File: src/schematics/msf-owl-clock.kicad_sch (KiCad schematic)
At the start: 55 parts, among them U001 BC805M, U002 TSOP75338TT

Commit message: Finalised various components and footprints.  Various tidy-ups.
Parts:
- added R017: 390Ω, restall-generic-resistors:nominal-0402-1005, symbol restall-generic-resistors:resistor
- CONN003: Manufacturer (none) -> Samtec; ManufacturerPartNumber (none) -> FTSH-105-01-L-DV-007-K
- CONN004: Manufacturer (none) -> Samtec; ManufacturerPartNumber (none) -> FTSH-110-01-F-DV-007-K
- LED001: footprint (none) -> restall-generic-leds:nominal-0603-1608; I_{F} ??mA_{typ} -> 20mA_{max}; Manufacturer (none) -> Harvatek; Manufacturer2 (none) -> Wurth Elektronik; Manufacturer2PartNumber (none) -> 150060RS75000; ManufacturerPartNumber (none) -> B1931USD-20D000814U1930; Package ??? -> 0603; V_{F} ?.?V_{typ} -> 2V_{typ}
- R004, R005, R007, R008, R009, R010, R011: value ??Ω -> 43Ω; Label ??Ω±1% 0.0625W -> 43Ω±1% 0.0625W
- R016: value 330Ω -> 390Ω; Label 330Ω±1% 0.0625W -> 390Ω±1% 0.0625W
- SPK001: value Speaker -> Header (Molex 502443-0270); footprint (none) -> restall-manufacturer-molex:502443-0270; Manufacturer (none) -> Molex; ManufacturerPartNumber (none) -> 502443-0270
- U001: footprint (none) -> restall-manufacturer-fanstel:BC805M
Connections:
- net 3-mcu-core/SDCARD_V_{DD}: now also R017.2
- net at LED001.2 (A), R016.1: now also R017.1
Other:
- note added: "R016-17"
- note added: "TODO: TFT CONNECTOR FOOTPRINTS..."
- note added: "The speaker should have a resonant frequency of less than 600Hz to cater for the lower-frequency bird sounds, such as the song of the tawny owl which has components around the 700Hz range. The speaker is connected to the PCB via a 2-pin header and pigtails. It is housed inside the clock's base / stand as that allows more freedom in the design of the cavity for better low-frequency response. This 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"
- note removed: "TODO: SELECT SPEAKER ! WILL PROBABLY NEED A SMALL ENCLOSURE OF SOME KIND (TO ABSORB THE OUT-OF-PHASE SOUND FROM BEHIND THE CONE AND ALLOW A DECENT LOW-FREQUENCY RESPONSE). MOUNTING ALSO NEEDS TO BE CONSIDERED - PREFERABLY ON THE BACK BUT WITH DIRECTION TO THE SIDE OR FRONT FOR BETTER AUDIO PROJECTION. PROBABLY A PART TO BUY AND/OR ASSEMBLE SEPARATELY RATHER THEN SEND FOR PCBA, SINCE NOT MANY SPEA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"
- moved on the sheet: LED001, SPK001

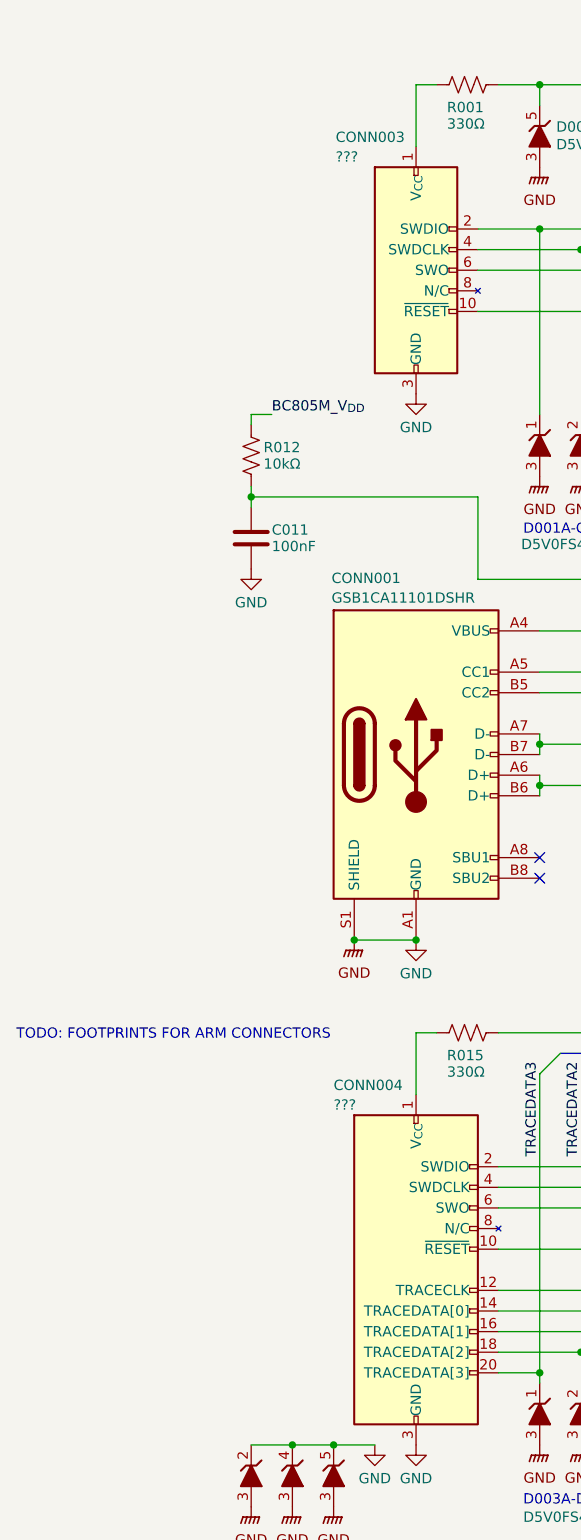
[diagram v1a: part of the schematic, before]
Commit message: Added footprints for the ARM debug connectors.  Added a datasheet for the speaker connector (Molex 502443-0270).
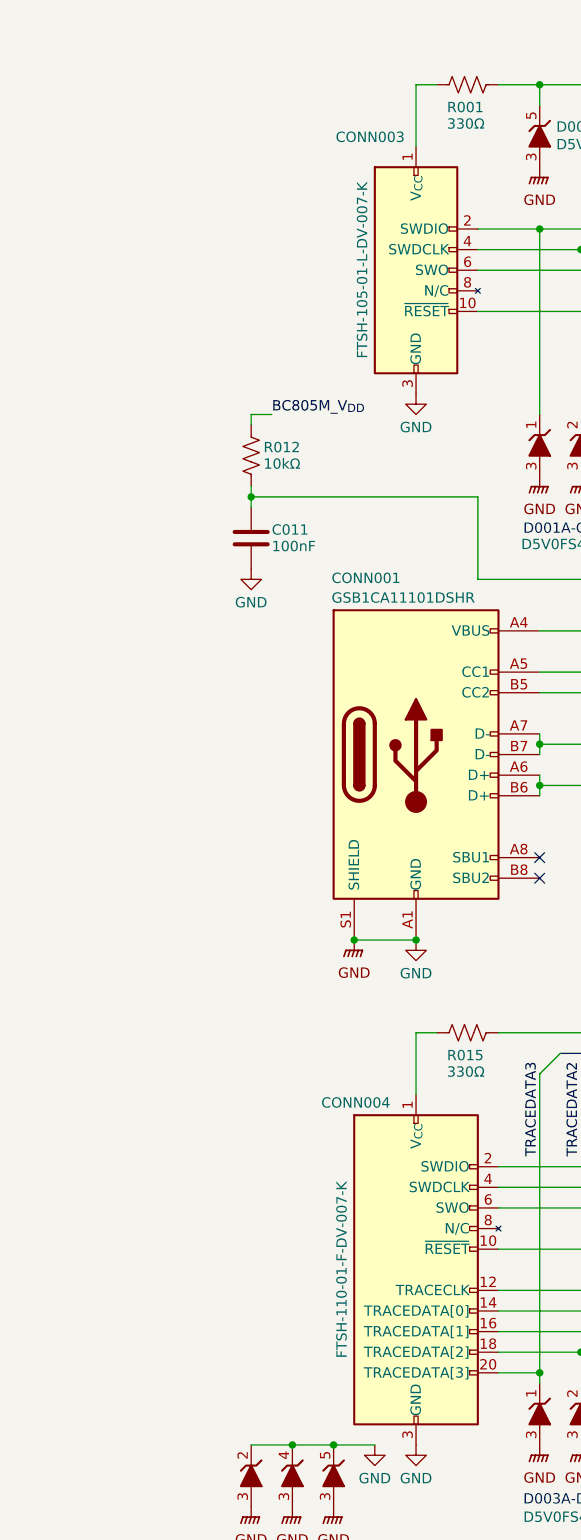
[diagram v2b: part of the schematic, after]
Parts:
- CONN003: footprint (none) -> restall-manufacturer-samtec:FTSH-105-?-?-DV-007-?-?; Package ??? -> FTSH-105-01-L-DV-007-K
- CONN004: footprint (none) -> restall-manufacturer-samtec:FTSH-110-01-?-DV-007-?-?; Package ??? -> FTSH-110-01-F-DV-007-K
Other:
- note removed: "TODO: FOOTPRINTS FOR ARM CONNECTORS"
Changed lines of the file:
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@@
     (effects (font (size 1.27 1.27)) (justify left bottom))
   )
-  (text "TODO: FOOTPRINTS FOR ARM CONNECTORS" (at -11.176 133.096 0)
-    (effects (font (size 1.27 1.27)) (justify left bottom))
-  )
   (text "TODO: DOUBLE-CHECK THESE PIN NUMBERS - THEY LOOK CORRECT BUT TRY AN ACTUAL CONNECTION (1 -> 12, 24 -> 13"
     (at 327.406 36.322 0)
@@
       (effects (font (size 1.27 1.27)) (justify left) hide)
     )
-    (property "Footprint" "" (at 38.1 34.29 0)
+    (property "Footprint" "restall-manufacturer-samtec:FTSH-105-?-?-DV-007-?-?" (at 38.1 34.29 0)
       (effects (font (size 1.27 1.27)) (justify left) hide)
     )
@@
       (effects (font (size 1.27 1.27)) (justify left) hide)
     )
-    (property "Package" "???" (at 28.194 24.13 0)
-      (effects (font (size 1.27 1.27)) (justify left))
+    (property "Package" "FTSH-105-01-L-DV-007-K" (at 31.496 38.1 90)
+      (effects (font (size 1.27 1.27)))
     )
     (property "Manufacturer" "Samtec" (at 38.1 33.02 0)
@@
   (symbol (lib_id "restall-manufacturer-arm:arm-cortex-m-debug-etm-header-2x10") (at 38.1 161.29 0) (unit 1)
     (in_bom yes) (on_board yes) (dnp no)
-    (property "Reference" "CONN004" (at 27.94 138.5458 0)
+    (property "Reference" "CONN004" (at 26.416 140.716 0)
       (effects (font (size 1.27 1.27)) (justify left))
     )
@@
       (effects (font (size 1.27 1.27)) (justify left) hide)
     )
-    (property "Footprint" "" (at 38.1 157.48 0)
+    (property "Footprint" "restall-manufacturer-samtec:FTSH-110-01-?-DV-007-?-?" (at 38.1 157.48 0)
       (effects (font (size 1.27 1.27)) (justify left) hide)
     )
@@
       (effects (font (size 1.27 1.27)) (justify left) hide)
     )
-    (property "Package" "???" (at 27.94 140.97 0)
-      (effects (font (size 1.27 1.27)) (justify left))
+    (property "Package" "FTSH-110-01-F-DV-007-K" (at 28.956 161.29 90)
+      (effects (font (size 1.27 1.27)))
     )
     (property "Manufacturer" "Samtec" (at 38.1 156.21 0)

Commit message: Added the USB connector footprint.
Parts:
- CONN001: footprint (none) -> restall-manufacturer-amphenol:GSB1CA11101DSHR
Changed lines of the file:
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@@
       (effects (font (size 1.27 1.27)) (justify left) hide)
     )
-    (property "Footprint" "" (at 44.45 116.84 0)
+    (property "Footprint" "restall-manufacturer-amphenol:GSB1CA11101DSHR" (at 44.45 116.84 0)
       (effects (font (size 1.27 1.27)) (justify left) hide)
     )

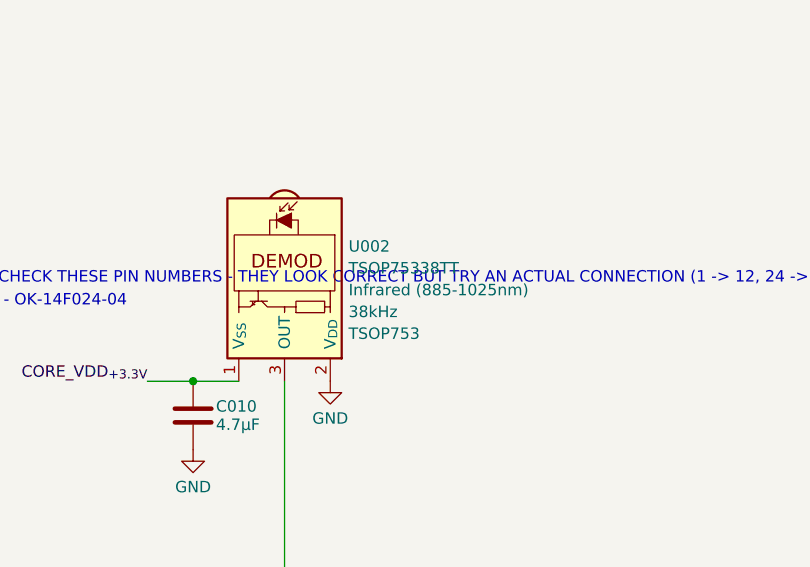
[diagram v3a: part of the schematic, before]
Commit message: Fixed the orientation of the TSOP75338TT.
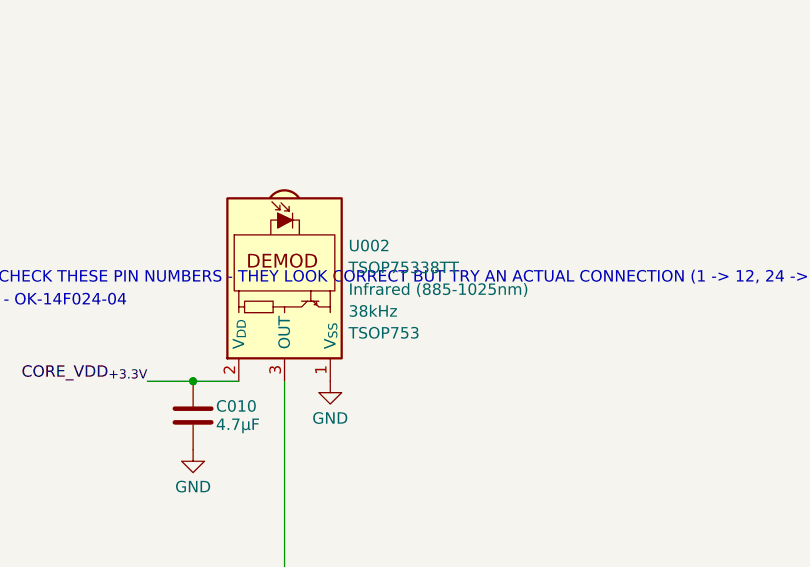
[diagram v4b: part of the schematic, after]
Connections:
- net CORE_VDD_{+3.3V}: now also U002.2 (V_{DD}); no longer U002.1 (V_{SS}), U002.4 (V_{SS})
- net GND: now also U002.1 (V_{SS}), U002.4 (V_{SS}); no longer U002.2 (V_{DD})
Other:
- moved on the sheet: U002
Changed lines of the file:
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@@
     )
   )
-  (symbol (lib_id "restall-manufacturer-vishay:TSOP75???T?") (at 373.38 36.83 270) (unit 1)
+  (symbol (lib_id "restall-manufacturer-vishay:TSOP75???T?") (at 373.38 36.83 90) (mirror x) (unit 1)
     (in_bom yes) (on_board yes) (dnp no)
-    (property "Reference" "U002" (at 380.492 32.004 90)
-      (effects (font (size 1.27 1.27)) (justify left))
+    (property "Reference" "U002" (at 380.492 31.9592 90)
+      (effects (font (size 1.27 1.27)) (justify right))
     )
-    (property "Value" "TSOP75338TT" (at 380.492 34.4282 90)
-      (effects (font (size 1.27 1.27)) (justify left))
+    (property "Value" "TSOP75338TT" (at 380.492 34.3834 90)
+      (effects (font (size 1.27 1.27)) (justify right))
     )
     (property "Footprint" "restall-manufacturer-vishay:TSOP7????TT" (at 373.38 30.48 90)
-      (effects (font (size 1.27 1.27)) (justify left) hide)
-    )
-    (property "Datasheet" "https://www.vishay.com/docs/82495/tsop753.pdf" (at 356.87 39.37 0)
       (effects (font (size 1.27 1.27)) (justify right) hide)
     )
-    (property "Wavelength" "Infrared (885-1025nm)" (at 380.492 36.8524 90)
-      (effects (font (size 1.27 1.27)) (justify left))
+    (property "Datasheet" "https://www.vishay.com/docs/82495/tsop753.pdf" (at 389.89 39.37 0)
+      (effects (font (size 1.27 1.27)) (justify right) hide)
     )
-    (property "Frequency" "38kHz" (at 380.492 39.2766 90)
-      (effects (font (size 1.27 1.27)) (justify left))
+    (property "Wavelength" "Infrared (885-1025nm)" (at 380.492 36.8076 90)
+      (effects (font (size 1.27 1.27)) (justify right))
     )
-    (property "Package" "TSOP753" (at 380.492 41.7008 90)
-      (effects (font (size 1.27 1.27)) (justify left))
+    (property "Frequency" "38kHz" (at 380.492 39.2318 90)
+      (effects (font (size 1.27 1.27)) (justify right))
     )
-    (property "Manufacturer" "Vishay" (at 360.934 39.37 0)
-      (effects (font (size 1.27 1.27)) (justify left) hide)
+    (property "Package" "TSOP753" (at 380.492 41.656 90)
+      (effects (font (size 1.27 1.27)) (justify right))
     )
-    (property "ManufacturerPartNumber" "TSOP75338TT" (at 358.902 39.37 0)
-      (effects (font (size 1.27 1.27)) (justify left) hide)
+    (property "Manufacturer" "Vishay" (at 385.826 39.37 0)
+      (effects (font (size 1.27 1.27)) (justify right) hide)
+    )
+    (property "ManufacturerPartNumber" "TSOP75338TT" (at 387.858 39.37 0)
+      (effects (font (size 1.27 1.27)) (justify right) hide)
     )
     (pin "2")

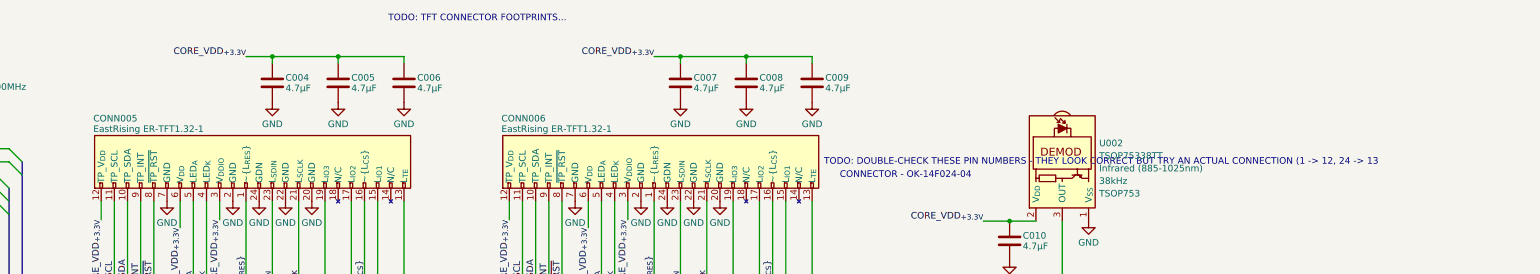
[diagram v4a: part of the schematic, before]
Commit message: Added the TFT connector footprints.
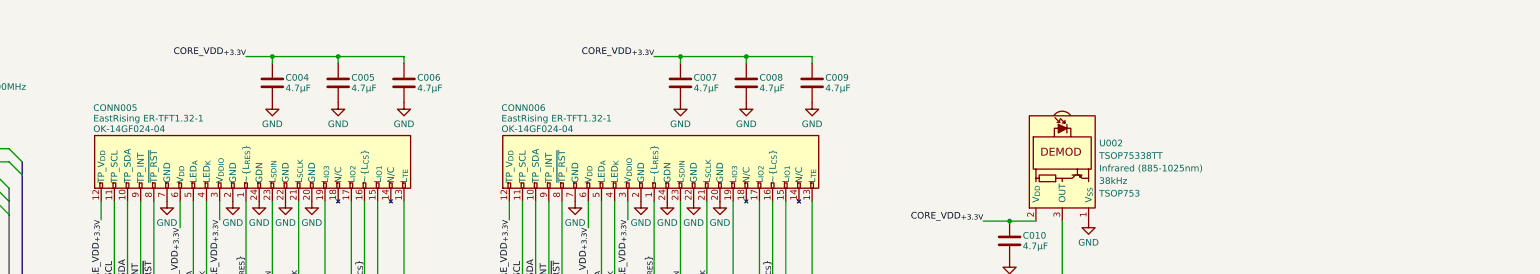
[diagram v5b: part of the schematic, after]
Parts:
- CONN005, CONN006: footprint (none) -> restall-manufacturer-eastrising:OK-14GF024-04; ManufacturerPartNumber ER-TFT1.32-1 -- NEEDS TO BE OK-14GF024-04 OR EQUIVALENT, IF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 -> OK-14GF024-04; Package (none) -> OK-14GF024-04
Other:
- note removed: "CONNECTOR - OK-14F024-04"
- note removed: "TODO: DOUBLE-CHECK THESE PIN NUMBERS - THEY LOOK CORRECT BUT TRY AN ACTUAL CONNECTION (1 -> 12, 24 -> 13"
- note removed: "TODO: TFT CONNECTOR FOOTPRINTS..."
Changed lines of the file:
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@@
-    (effects (font (size 1.27 1.27)) (justify left bottom))
-  )
-  (text "TODO: TFT CONNECTOR FOOTPRINTS..." (at 243.332 8.636 0)
     (effects (font (size 1.27 1.27)) (justify left bottom))
   )
@@
     (effects (font (size 1.27 1.27)) (justify left bottom))
   )
-  (text "TODO: DOUBLE-CHECK THESE PIN NUMBERS - THEY LOOK CORRECT BUT TRY AN ACTUAL CONNECTION (1 -> 12, 24 -> 13"
-    (at 327.406 36.322 0)
-    (effects (font (size 1.27 1.27)) (justify left bottom))
-  )
   (text "D004B-D" (at 15.494 198.12 0)
-    (effects (font (size 1.27 1.27)) (justify left bottom))
-  )
-  (text "CONNECTOR - OK-14F024-04" (at 330.454 38.862 0)
     (effects (font (size 1.27 1.27)) (justify left bottom))
   )
@@
   (symbol (lib_id "restall-manufacturer-eastrising:ER-TFT1.32-1-reversed-direct-layout") (at 217.17 35.56 90) (unit 1)
     (in_bom yes) (on_board yes) (dnp no)
-    (property "Reference" "CONN005" (at 186.436 27.178 90)
+    (property "Reference" "CONN005" (at 186.436 25.146 90)
       (effects (font (size 1.27 1.27)) (justify right))
     )
-    (property "Value" "EastRising ER-TFT1.32-1" (at 186.436 29.21 90)
+    (property "Value" "EastRising ER-TFT1.32-1" (at 186.436 27.178 90)
       (effects (font (size 1.27 1.27)) (justify right))
     )
-    (property "Footprint" "" (at 193.04 38.1 0)
+    (property "Footprint" "restall-manufacturer-eastrising:OK-14GF024-04" (at 193.04 38.1 0)
       (effects (font (size 1.27 1.27)) (justify left) hide)
     )
@@
       (effects (font (size 1.27 1.27)) (justify left) hide)
     )
-    (property "ManufacturerPartNumber" "ER-TFT1.32-1 -- NEEDS TO BE OK-14GF024-04 OR EQUIVALENT, IF CAN FIND A 0.4mm 24-WAY FEMALE FPC !" (at 256.54 35.56 0)
-      (effects (font (size 1.27 1.27)) (justify left) hide)
+    (property "ManufacturerPartNumber" "OK-14GF024-04" (at 256.54 35.56 0)
+      (effects (font (size 1.27 1.27)) (justify left) hide)
+    )
+    (property "Package" "OK-14GF024-04" (at 186.436 29.21 90)
+      (effects (font (size 1.27 1.27)) (justify right))
     )
     (pin "23")
@@
   (symbol (lib_id "restall-manufacturer-eastrising:ER-TFT1.32-1-reversed-direct-layout") (at 295.91 35.56 90) (unit 1)
     (in_bom yes) (on_board yes) (dnp no)
-    (property "Reference" "CONN006" (at 265.176 27.178 90)
+    (property "Reference" "CONN006" (at 265.176 25.146 90)
       (effects (font (size 1.27 1.27)) (justify right))
     )
-    (property "Value" "EastRising ER-TFT1.32-1" (at 265.176 29.21 90)
+    (property "Value" "EastRising ER-TFT1.32-1" (at 265.176 27.178 90)
       (effects (font (size 1.27 1.27)) (justify right))
     )
-    (property "Footprint" "" (at 271.78 38.1 0)
+    (property "Footprint" "restall-manufacturer-eastrising:OK-14GF024-04" (at 271.78 38.1 0)
       (effects (font (size 1.27 1.27)) (justify left) hide)
     )
@@
       (effects (font (size 1.27 1.27)) (justify left) hide)
     )
-    (property "ManufacturerPartNumber" "ER-TFT1.32-1 -- NEEDS TO BE OK-14GF024-04 OR EQUIVALENT, IF CAN FIND A 0.4mm 24-WAY FEMALE FPC !" (at 335.28 35.56 0)
-      (effects (font (size 1.27 1.27)) (justify left) hide)
+    (property "ManufacturerPartNumber" "OK-14GF024-04" (at 335.28 35.56 0)
+      (effects (font (size 1.27 1.27)) (justify left) hide)
+    )
+    (property "Package" "OK-14GF024-04" (at 265.176 29.21 90)
+      (effects (font (size 1.27 1.27)) (justify right))
     )
     (pin "23")

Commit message: Added the SD Card connector's (MSD-11-A) footprint.
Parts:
- CONN002: footprint (none) -> restall-manufacturer-cui:MSD-11-A
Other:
- note added: "TODO: ANTENNA FOOTPRINT !"
- note added: "TODO: FOOTPRINTS FOR THE EYES - NO SYMBOL REQUIRED, HOWEVER."
- note removed: "TODO: FOOTPRINT FOR SD CARD !"
- moved on the sheet: ANT001, C001, C002, C003, C004, C005, C006, C007, C008, C009, C010, C011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

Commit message: Updated the ferrite rod antenna symbol.
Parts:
- ANT001: footprint (none) -> msf-owl-clock:ferrite-rod-antenna
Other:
- note removed: "TODO: ANTENNA FOOTPRINT !"
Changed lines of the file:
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@@
     (effects (font (size 1.27 1.27)) (justify left bottom))
   )
-  (text "TODO: ANTENNA FOOTPRINT !" (at 245.872 279.146 0)
-    (effects (font (size 1.27 1.27)) (justify left bottom))
-  )
   (label "DAT1" (at 105.41 213.36 0) (fields_autoplaced)
     (effects (font (size 1.27 1.27)) (justify left bottom))
@@
       (effects (font (size 1.27 1.27)))
     )
-    (property "Footprint" "" (at 248.92 261.62 90)
+    (property "Footprint" "msf-owl-clock:ferrite-rod-antenna" (at 248.92 261.62 90)
       (effects (font (size 1.27 1.27)) (justify left) hide)
     )
